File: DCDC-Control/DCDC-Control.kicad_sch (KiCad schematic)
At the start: 0 parts

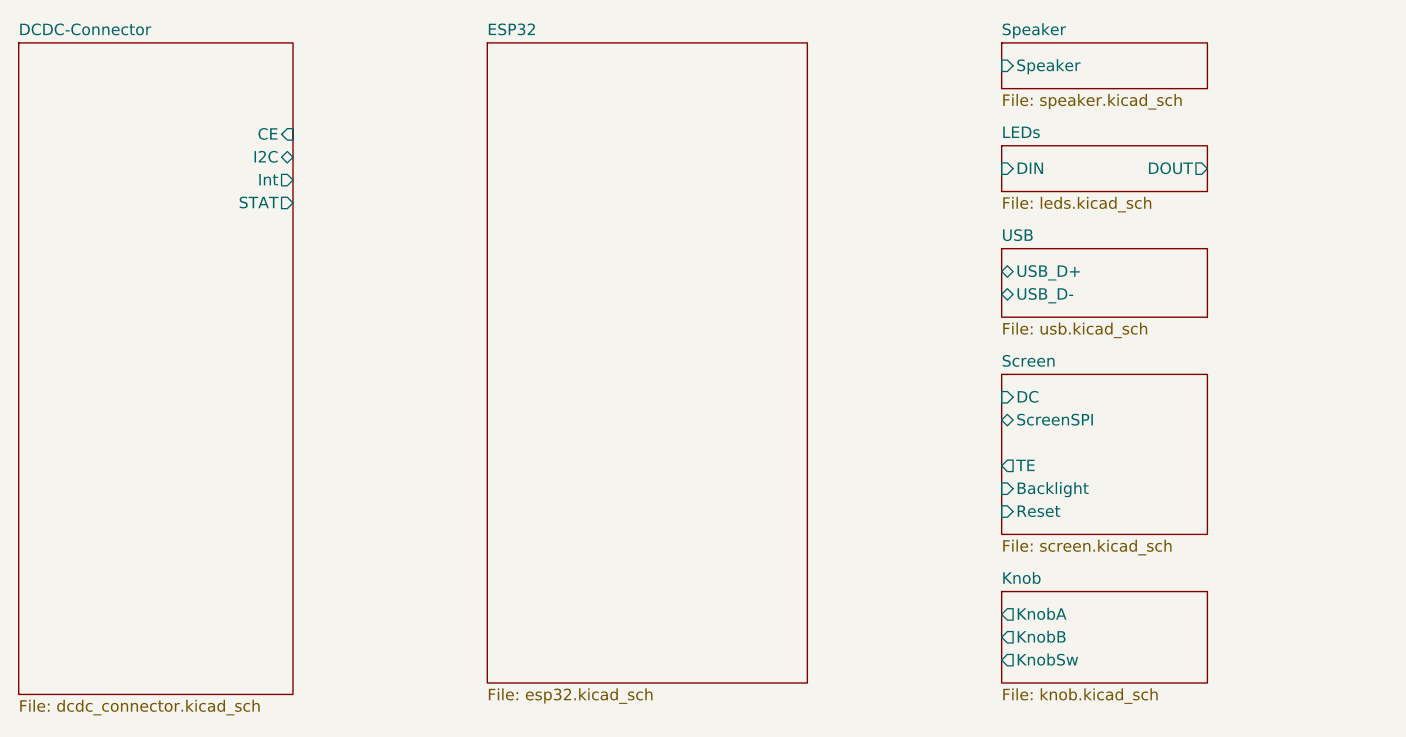
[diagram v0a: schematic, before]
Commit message: almost finished control schematics
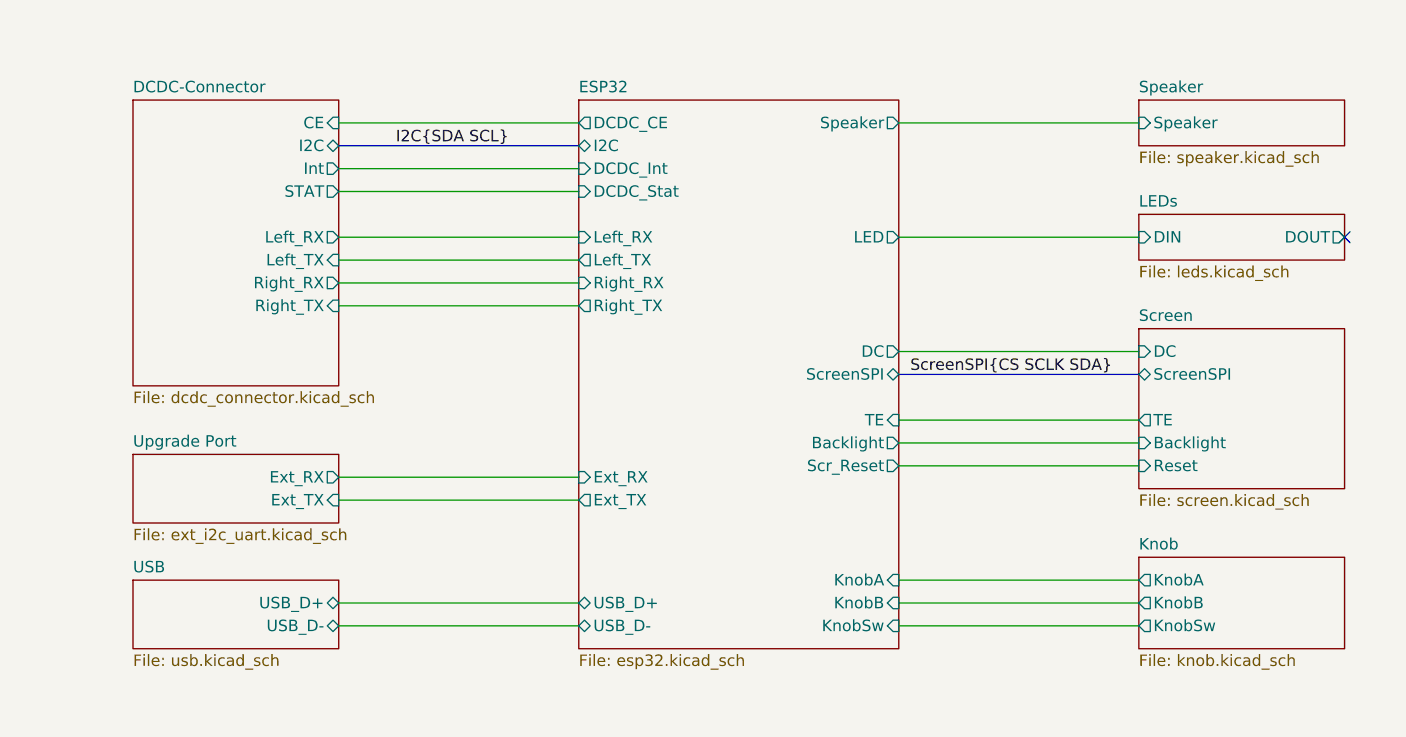
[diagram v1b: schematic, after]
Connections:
- no-connect marks 0 -> 1
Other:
- added sheet Upgrade Port (ext_i2c_uart.kicad_sch)
- sheet DCDC-Connector ports: added Left_RX, Left_TX, Right_RX, Right_TX; removed none
- sheet ESP32 ports: added Backlight, DC, DCDC_CE, DCDC_Int, DCDC_Stat, Ext_RX, Ext_TX, I2C, KnobA, KnobB, KnobSw, LED, Left_RX, Left_TX, Right_RX, Right_TX, Scr_Reset, ScreenSPI, Speaker, TE, USB_D+, USB_D-; removed none

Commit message: some DCDC schematics
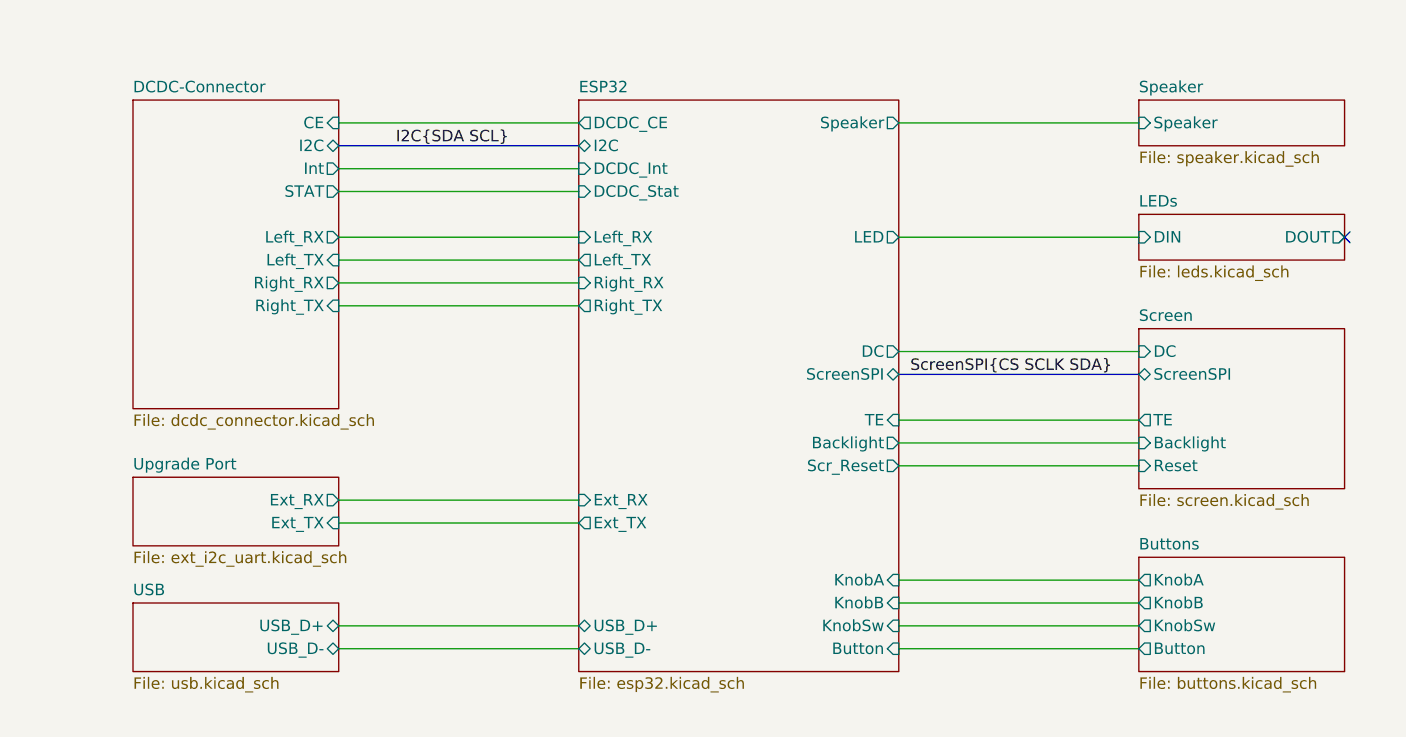
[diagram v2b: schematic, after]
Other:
- sheet Knob renamed Buttons
- sheet Buttons: file knob.kicad_sch -> buttons.kicad_sch
- sheet Buttons ports: added Button; removed none
- sheet ESP32 ports: added Button; removed none
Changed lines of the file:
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@@
+	(wire
+		(pts
+			(xy 63.5 76.2) (xy 90.17 76.2)
+		)
+		(stroke
+			(width 0)
+			(type default)
+		)
+	)
+	(wire
+		(pts
+			(xy 63.5 31.75) (xy 90.17 31.75)
+		)
+		(stroke
+			(width 0)
+			(type default)
+		)
+	)
+	(wire
+		(pts
+			(xy 125.73 31.75) (xy 152.4 31.75)
+		)
+		(stroke
+			(width 0)
+			(type default)
+		)
+	)
+	(wire
+		(pts
+			(xy 63.5 44.45) (xy 90.17 44.45)
+		)
+		(stroke
+			(width 0)
+			(type default)
+		)
+	)
+	(wire
+		(pts
+			(xy 63.5 87.63) (xy 90.17 87.63)
+		)
+		(stroke
+			(width 0)
+			(type default)
+		)
+	)
+	(wire
+		(pts
+			(xy 63.5 90.17) (xy 90.17 90.17)
+		)
+		(stroke
+			(width 0)
+			(type default)
+		)
+	)
+	(wire
+		(pts
+			(xy 63.5 52.07) (xy 90.17 52.07)
+		)
+		(stroke
+			(width 0)
+			(type default)
+		)
+	)
 	(wire
 		(pts
@@
 	(wire
 		(pts
-			(xy 63.5 31.75) (xy 90.17 31.75)
-		)
-		(stroke
-			(width 0)
-			(type default)
-		)
-	)
-	(wire
-		(pts
-			(xy 125.73 31.75) (xy 152.4 31.75)
-		)
-		(stroke
-			(width 0)
-			(type default)
-		)
-	)
-	(wire
-		(pts
-			(xy 63.5 44.45) (xy 90.17 44.45)
-		)
-		(stroke
-			(width 0)
-			(type default)
-		)
-	)
-	(wire
-		(pts
-			(xy 63.5 85.09) (xy 90.17 85.09)
-		)
-		(stroke
-			(width 0)
-			(type default)
-		)
-	)
-	(wire
-		(pts
-			(xy 63.5 87.63) (xy 90.17 87.63)
-		)
-		(stroke
-			(width 0)
-			(type default)
-		)
-	)
-	(wire
-		(pts
-			(xy 63.5 52.07) (xy 90.17 52.07)
-		)
-		(stroke
-			(width 0)
-			(type default)
-		)
-	)
-	(wire
-		(pts
-			(xy 63.5 71.12) (xy 90.17 71.12)
-		)
-		(stroke
-			(width 0)
-			(type default)
-		)
-	)
-	(wire
-		(pts
 			(xy 125.73 69.85) (xy 152.4 69.85)
+		)
+		(stroke
+			(width 0)
+			(type default)
+		)
+	)
+	(wire
+		(pts
+			(xy 125.73 90.17) (xy 152.4 90.17)
 		)
 		(stroke
@@
 	(sheet
 		(at 90.17 29.21)
-		(size 35.56 60.96)
+		(size 35.56 63.5)
 		(exclude_from_sim no)
 		(in_bom yes)
@@
 		)
 		(property "Sheetfile" "esp32.kicad_sch"
-			(at 90.17 90.7546 0)
+			(at 90.17 93.2946 0)
 			(effects
 				(font
@@
 		)
 		(pin "USB_D+" bidirectional
-			(at 90.17 85.09 180)
+			(at 90.17 87.63 180)
 			(effects
 				(font
@@
 		)
 		(pin "USB_D-" bidirectional
-			(at 90.17 87.63 180)
+			(at 90.17 90.17 180)
 			(effects
 				(font
@@
 		)
 		(pin "Ext_RX" input
-			(at 90.17 71.12 180)
+			(at 90.17 73.66 180)
 			(effects
 				(font
@@
 		)
 		(pin "Ext_TX" output
-			(at 90.17 73.66 180)
+			(at 90.17 76.2 180)
 			(effects
 				(font
@@
 				)
 				(justify left)
+			)
+		)
+		(pin "Button" input
+			(at 125.73 90.17 0)
+			(effects
+				(font
+					(size 1.27 1.27)
+				)
+				(justify right)
 			)
 		)
@@
 	)
 	(sheet
-		(at 40.64 68.58)
+		(at 40.64 71.12)
 		(size 22.86 7.62)
 		(exclude_from_sim no)
@@
 		)
 		(property "Sheetname" "Upgrade Port"
-			(at 40.64 67.8684 0)
+			(at 40.64 70.4084 0)
 			(effects
 				(font
@@
 		)
 		(property "Sheetfile" "ext_i2c_uart.kicad_sch"
-			(at 40.64 76.7846 0)
+			(at 40.64 79.3246 0)
 			(effects
 				(font
@@
 		)
 		(pin "Ext_RX" output
-			(at 63.5 71.12 0)
+			(at 63.5 73.66 0)
 			(effects
 				(font
@@
 		)
 		(pin "Ext_TX" input
-			(at 63.5 73.66 0)
+			(at 63.5 76.2 0)
 			(effects
 				(font
@@
 	(sheet
 		(at 152.4 80.01)
-		(size 22.86 10.16)
+		(size 22.86 12.7)
 		(exclude_from_sim no)
 		(in_bom yes)
@@
 			(color 0 0 0 0.0000)
 		)
-		(property "Sheetname" "Knob"
+		(property "Sheetname" "Buttons"
 			(at 152.4 79.2984 0)
 			(effects
@@
 			)
 		)
-		(property "Sheetfile" "knob.kicad_sch"
-			(at 152.4 90.7546 0)
+		(property "Sheetfile" "buttons.kicad_sch"
+			(at 152.4 93.2946 0)
 			(effects
 				(font
@@
 		(pin "KnobSw" output
 			(at 152.4 87.63 180)
+			(effects
+				(font
+					(size 1.27 1.27)
+				)
+				(justify left)
+			)
+		)
+		(pin "Button" output
+			(at 152.4 90.17 180)
 			(effects
 				(font
@@
 	(sheet
 		(at 40.64 29.21)
-		(size 22.86 31.75)
+		(size 22.86 34.29)
 		(exclude_from_sim no)
 		(in_bom yes)
@@
 		)
 		(property "Sheetfile" "dcdc_connector.kicad_sch"
-			(at 40.64 61.5446 0)
+			(at 40.64 64.0846 0)
 			(effects
 				(font
@@
 	)
 	(sheet
-		(at 40.64 82.55)
+		(at 40.64 85.09)
 		(size 22.86 7.62)
 		(exclude_from_sim no)
@@
 		)
 		(property "Sheetname" "USB"
-			(at 40.64 81.8384 0)
+			(at 40.64 84.3784 0)
 			(effects
 				(font
@@
 		)
 		(property "Sheetfile" "usb.kicad_sch"
-			(at 40.64 90.7546 0)
+			(at 40.64 93.2946 0)
 			(effects
 				(font
@@
 		)
 		(pin "USB_D+" bidirectional
-			(at 63.5 85.09 0)
+			(at 63.5 87.63 0)
 			(effects
 				(font
@@
 		)
 		(pin "USB_D-" bidirectional
-			(at 63.5 87.63 0)
-			(effects
-				(font
+			(at 63.5 90.17 0)
+			(effects
+				(font
